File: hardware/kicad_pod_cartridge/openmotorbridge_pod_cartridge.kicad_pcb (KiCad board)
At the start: 2 copper layers, 35 x 25 mm, 9 parts

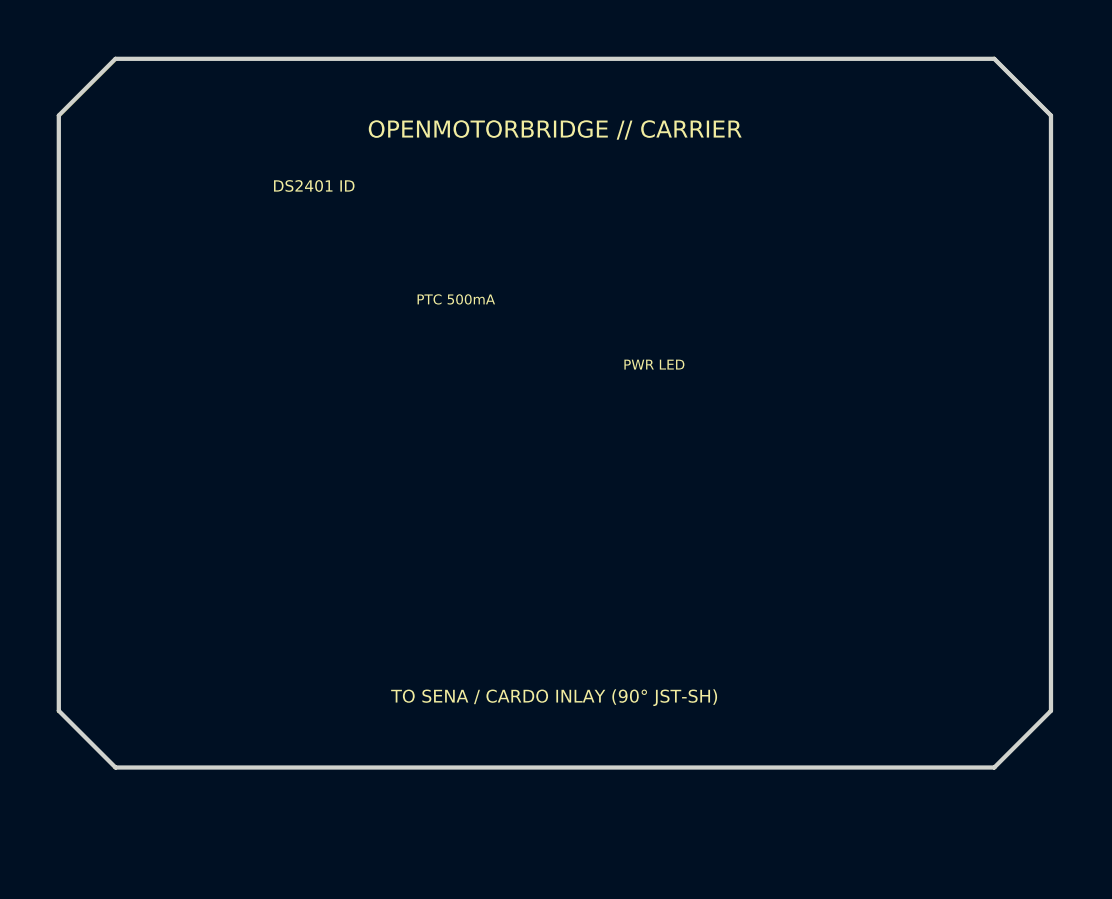
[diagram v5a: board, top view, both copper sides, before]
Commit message: hardware(cad/renders): update 3D board renders and mechanical CAD assembly for centric cartridge sled and horizontal mating
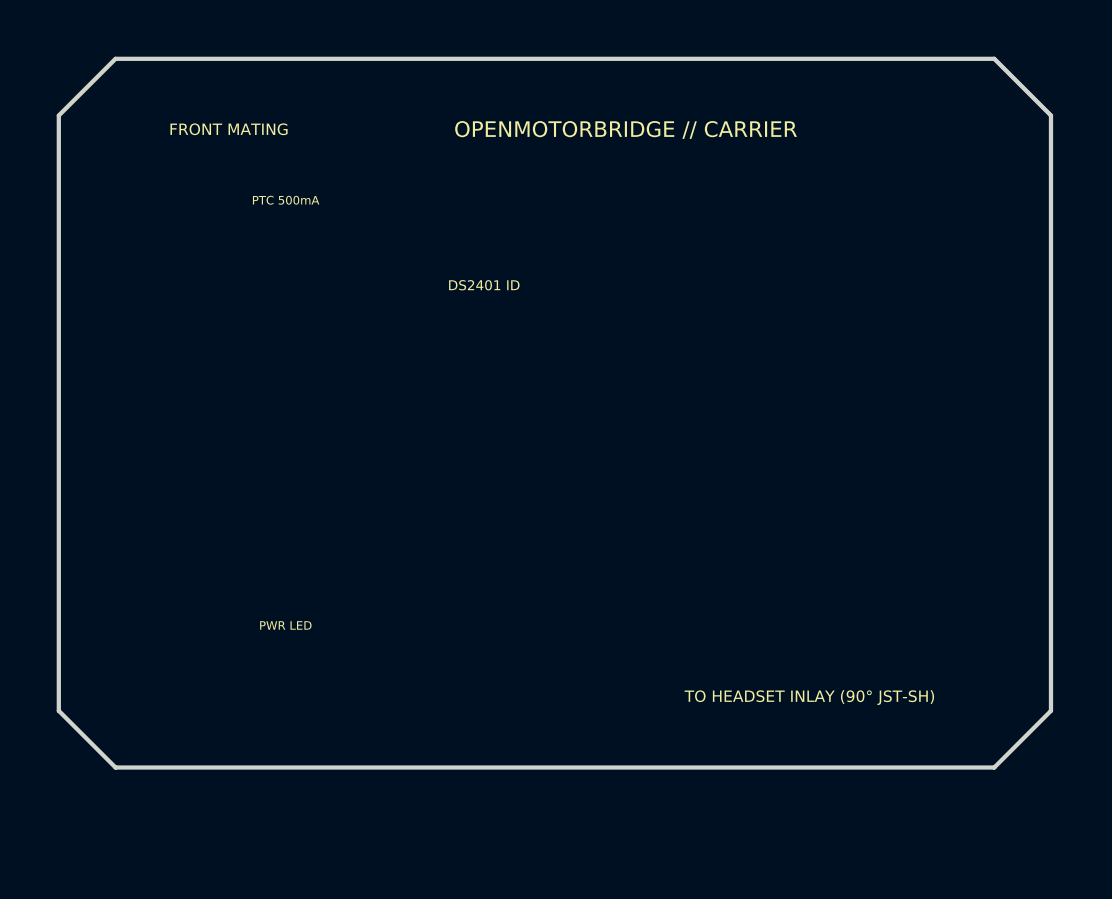
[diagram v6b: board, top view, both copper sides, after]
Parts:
- J1: moved to F.Cu
- moved H2 30.0 mm to (103.0, 89.5)
- moved D1 17.4 mm to (108.0, 85.0)
- moved J1 16.3 mm to (102.5, 73.7)
- moved R1 14.5 mm to (108.0, 82.5)
- moved H1 9.51 mm to (103.0, 70.5)
- moved U1 7.50 mm to (115.0, 80.0)
- moved F1 6.18 mm to (108.0, 75.0)
- moved C1 6.00 mm to (115.0, 84.5)
- moved J2 0.50 mm to (126.5, 80.0)
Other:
- board text added: "FRONT MATING"
- board text added: "OPENMOTORBRIDGE CARRIER (B.Cu)"
- board text added: "TO HEADSET INLAY (90° JST-SH)"
- board text removed: "6-PIN SOCKET (MATES TO POD-BASE)"
- board text removed: "TO SENA / CARDO INLAY (90° JST-SH)"
